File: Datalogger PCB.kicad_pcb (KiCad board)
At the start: 2 copper layers, 56.4 x 37.1 mm, 29 parts, among them J1 Conn_01x04_Pin, J2 Conn_01x04_Pin, J3 Conn_01x09_Pin, J4 Conn_02x03_Odd_Even, U1 24LC1025, U2 24LC1025, U3 ATmega328-P, U4 DS1337S_T_R, Y1 32.768 kHz, Y2 16MHz

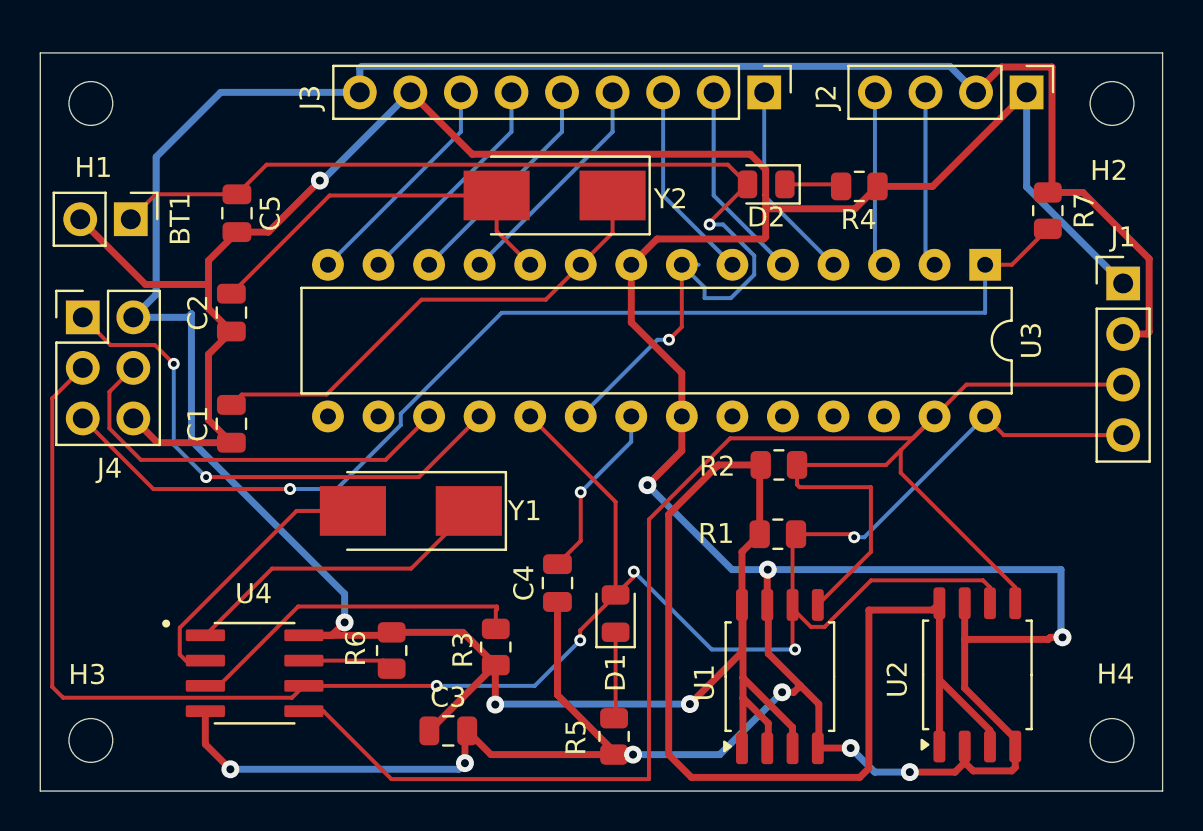
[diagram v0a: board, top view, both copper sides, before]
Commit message: Added silkscreen
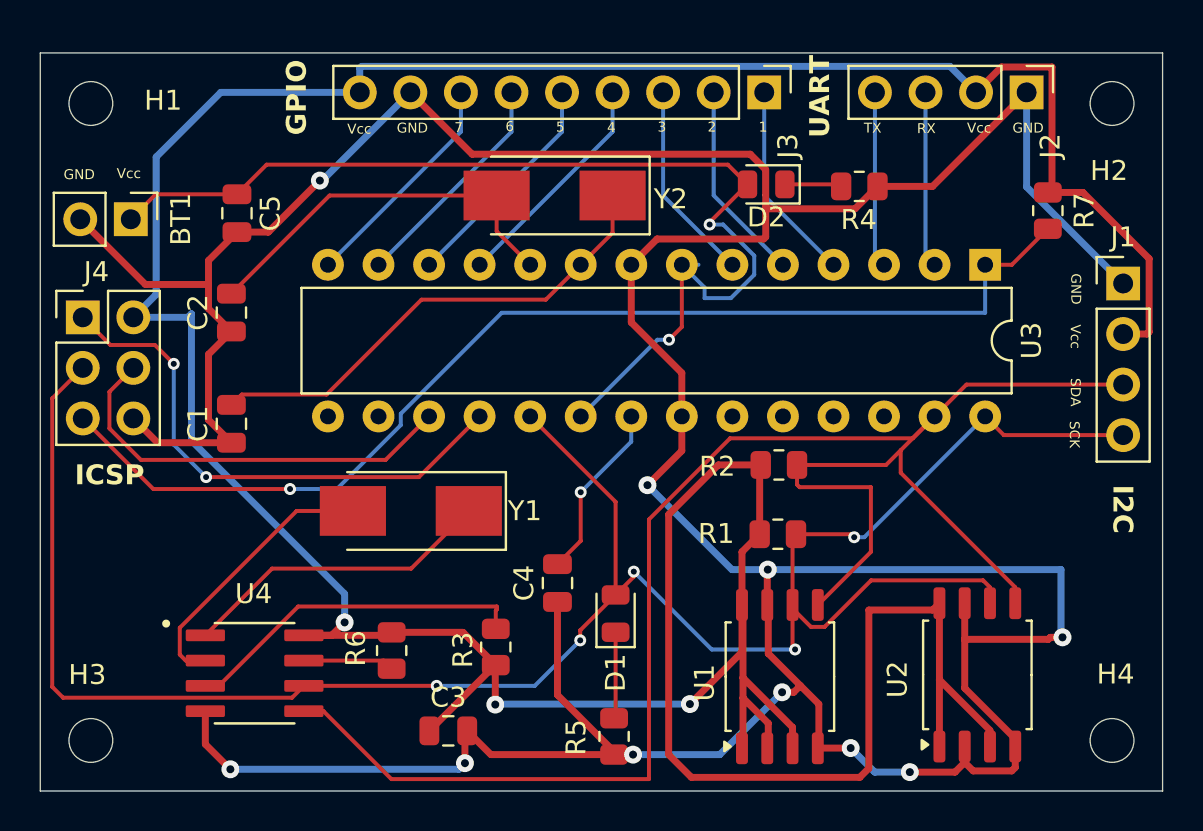
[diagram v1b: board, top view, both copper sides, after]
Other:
- board text added: "1"
- board text added: "2"
- board text added: "3"
- board text added: "4"
- board text added: "5"
- board text added: "6"
- board text added: "7"
- board text added: "GND"
- board text added: "GPIO"
- board text added: "I2C"
- board text added: "ICSP"
- board text added: "RX"
- board text added: "SCK"
- board text added: "SDA"
- board text added: "TX"
- board text added: "UART"
- board text added: "Vcc"
